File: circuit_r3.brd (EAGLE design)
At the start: 57.3 x 43.2 mm, 24 parts, among them IC1 7805DT, U1 MCP4725, U2 MB85RC256VPF-G-JNERE2, U4 ATMEGA328P_VQFNVQFN, Y1 16MHz

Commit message: Oooh, getting close.
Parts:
- removed C7: 0.1uF, custom:0603
- added J1: (no value), SparkFun-Connectors:6_PIN_SERIAL_TARGET_SIDE_W_SILK
- moved C5 90.6 mm to (47.0, 47.0), turned to 180 degrees
- moved C6 89.5 mm to (47.0, 41.9), turned to 180 degrees
- moved R5 85.0 mm to (47.0, 44.5), turned to 180 degrees
- moved C2 62.9 mm to (68.6, 39.2), turned to 270 degrees
- moved R1 62.6 mm to (61.2, 31.5), turned to 315 degrees
- moved U1 60.8 mm to (65.8, 39.0), turned to 270 degrees
- moved U2 58.9 mm to (62.2, 43.2), turned to 90 degrees
- moved R4 56.8 mm to (65.8, 35.4), turned to 180 degrees
- moved 12V 52.7 mm to (54.6, 24.1)
- moved U4 50.4 mm to (57.1, 35.6), turned to 45 degrees
- moved C4 46.7 mm to (61.6, 26.6), turned to 45 degrees
- moved R3 46.0 mm to (58.4, 47.0), turned to 90 degrees
- moved R6 45.7 mm to (56.4, 31.9), turned to 225 degrees
- moved ETH_PWR 45.1 mm to (50.8, 24.1)
- moved Y1 44.1 mm to (59.1, 29.2), turned to 135 degrees
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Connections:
- removed net AREF: C7.1, U4.17
- new net RXI: J1.P$2, U4.26
- new net TXO: J1.P$3, U4.27
- net DTR: now also J1.P$1
- net GND: now also J1.P$5, J1.P$6; no longer C7.2
- net VCC: now also J1.P$4
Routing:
- net GND: track 0.00 -> 48.2 mm, vias 0 -> 5
- net VCC: track 0.00 -> 31.7 mm, vias 0 -> 6
- net OUT: track 0.00 -> 26.4 mm, vias 0 -> 1
- net SCL: track 0.00 -> 26.1 mm, vias 0 -> 2
- net ETH: track 0.00 -> 24.9 mm, vias 0 -> 1
- net SDA: track 0.00 -> 19.5 mm
- net TXO: track 0.00 -> 14.7 mm, vias 0 -> 1
- net RXI: track 0.00 -> 13.3 mm, vias 0 -> 1
- net RESET: track 0.00 -> 12.9 mm
- net XT2: track 0.00 -> 11.7 mm
- net DTR: track 0.00 -> 10.8 mm
- net XT1: track 0.00 -> 9.59 mm
- net VIN: track 0.00 -> 9.25 mm
- net PD_L: track 0.00 -> 2.79 mm
- added copper zone on layer 2, net GND
- added copper zone on layer 15, net VCC
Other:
- board size 57.3 x 43.2 mm -> 160 x 100 mm

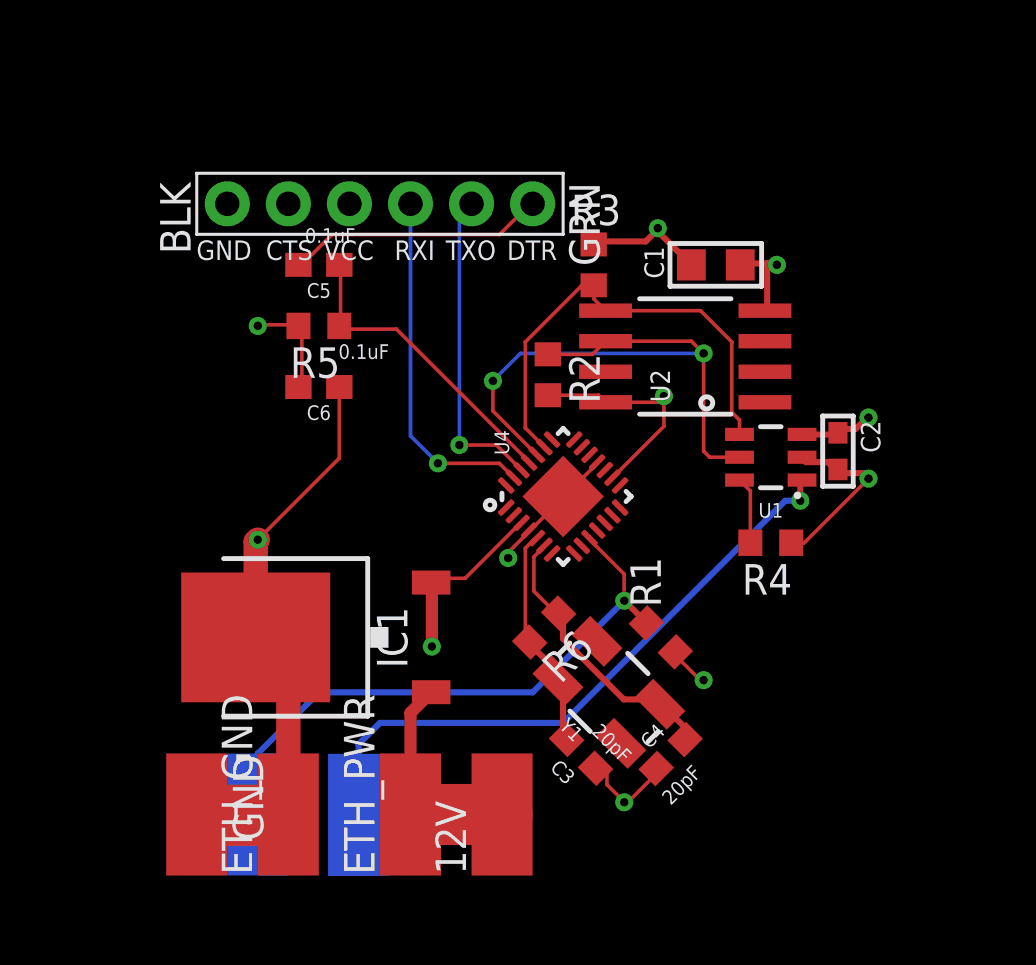
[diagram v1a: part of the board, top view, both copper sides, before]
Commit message: trying to make it smaller.
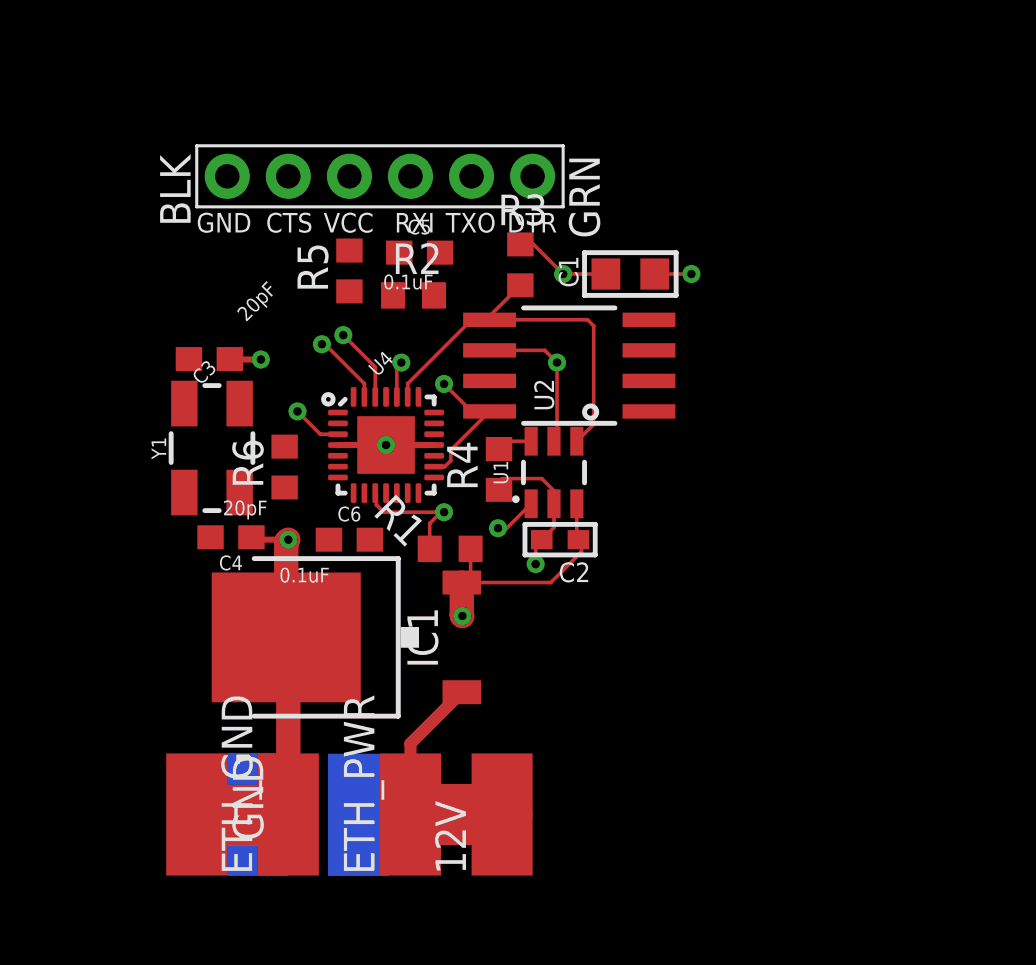
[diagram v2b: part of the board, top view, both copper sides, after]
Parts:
- moved C3 22.6 mm to (42.4, 43.1), turned to 180 degrees
- moved C4 20.4 mm to (43.3, 35.7), turned to 180 degrees
- moved Y1 19.4 mm to (42.5, 39.4), turned to 90 degrees
- moved R6 12.7 mm to (45.6, 38.6), turned to 90 degrees
- moved C2 12.1 mm to (57.0, 35.6), turned to 180 degrees
- moved R4 11.7 mm to (54.5, 38.5), turned to 90 degrees
- moved R1 9.51 mm to (52.5, 35.2), turned to 0 degrees
- moved U1 9.04 mm to (56.8, 38.4), turned to 180 degrees
- moved U4 9.04 mm to (48.5, 38.2), turned to 0 degrees
- moved R2 6.49 mm to (50.9, 45.7), turned to 0 degrees
- moved C6 6.48 mm to (48.3, 35.6), turned to 0 degrees
- moved U2 4.84 mm to (57.4, 42.8)
- moved C5 4.22 mm to (51.2, 47.5), turned to 0 degrees
- moved C1 3.58 mm to (59.9, 46.6)
- moved R3 3.05 mm to (55.4, 47.0)
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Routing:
- net OUT: track 26.4 -> 1.80 mm
- net ETH: track 24.9 -> 5.17 mm
- net SCL: track 26.1 -> 7.85 mm
- net GND: track 48.2 -> 32.3 mm
- net RESET: track 12.9 -> 0.00 mm
- net XT2: track 11.7 -> 0.00 mm
- net TXO: track 14.7 -> 3.00 mm
- net DTR: track 10.8 -> 0.00 mm
- net XT1: track 9.59 -> 0.00 mm
- net RXI: track 13.3 -> 3.84 mm
- net VCC: track 31.7 -> 22.8 mm, vias 6 -> 4
- net SDA: track 19.5 -> 15.6 mm
- net PD_L: track 2.79 -> 1.47 mm
- net VIN: track 9.25 -> 9.78 mm

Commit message: pre autoroute
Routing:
- net ETH: track 5.17 -> 21.0 mm
- net OUT: track 1.80 -> 16.1 mm
- net TXO: track 3.00 -> 11.5 mm
- net RXI: track 3.84 -> 11.9 mm
- net RESET: track 0.00 -> 5.02 mm
- net SCL: track 7.85 -> 10.8 mm
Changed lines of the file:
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@@
 <wire x1="56.896" y1="42.926" x2="56.896" y2="39.7811" width="0.1524" layer="1"/>
 <wire x1="56.896" y1="39.7811" x2="56.769" y2="39.6541" width="0.1524" layer="1"/>
-<wire x1="50.419" y1="42.926" x2="50.077" y2="45.72" width="0" layer="19" extent="1-1"/>
-<wire x1="54.089" y1="43.434" x2="50.419" y2="42.926" width="0" layer="19" extent="1-1"/>
+<wire x1="50.077" y1="45.72" x2="50.419" y2="45.378" width="0.1524" layer="1"/>
+<wire x1="50.419" y1="45.378" x2="50.419" y2="42.926" width="0.1524" layer="1"/>
+<wire x1="50.419" y1="42.926" x2="54.089" y2="43.434" width="0" layer="19" extent="1-1"/>
 </signal>
 <signal name="ETH">
@@
 <wire x1="51.601" y1="35.179" x2="51.601" y2="36.234" width="0.1524" layer="1"/>
 <wire x1="51.601" y1="36.234" x2="52.07" y2="36.703" width="0.1524" layer="1"/>
-<wire x1="44.45" y1="24.13" x2="51.601" y2="35.179" width="0" layer="19" extent="1-16"/>
+<wire x1="52.197" y1="36.703" x2="52.197" y2="34.417" width="0.1524" layer="16"/>
+<wire x1="52.197" y1="34.417" x2="44.45" y2="26.67" width="0.1524" layer="16"/>
+<wire x1="44.45" y1="26.67" x2="44.45" y2="24.13" width="0.1524" layer="16"/>
 </signal>
 <signal name="PD_L">
@@
 <wire x1="55.819" y1="37.0539" x2="54.8011" y2="36.036" width="0.1524" layer="1"/>
 <wire x1="54.8011" y1="36.036" x2="54.441" y2="36.036" width="0.1524" layer="1"/>
-<wire x1="48.641" y1="24.111946875" x2="54.441" y2="36.036" width="0" layer="19" extent="16-16"/>
+<wire x1="54.441" y1="36.036" x2="54.441" y2="29.911946875" width="0.1524" layer="16"/>
+<wire x1="54.441" y1="29.911946875" x2="48.641" y2="24.111946875" width="0.1524" layer="16"/>
 </signal>
 <signal name="XT1">
@@
 <contactref element="C5" pad="1"/>
 <contactref element="U4" pad="25"/>
-<wire x1="50.331" y1="47.498" x2="48.26" y2="45.886" width="0" layer="19" extent="1-1"/>
-<wire x1="49.784" y1="41.497" x2="48.26" y2="45.886" width="0" layer="19" extent="1-1"/>
+<wire x1="49.784" y1="41.497" x2="49.7352" y2="41.5458" width="0.1524" layer="1"/>
+<wire x1="48.26" y1="44.7475375" x2="48.26" y2="45.886" width="0.1524" layer="1"/>
+<wire x1="49.7352" y1="41.5458" x2="49.7352" y2="43.2723375" width="0.1524" layer="1"/>
+<wire x1="49.7352" y1="43.2723375" x2="48.26" y2="44.7475375" width="0.1524" layer="1"/>
+<wire x1="48.26" y1="45.886" x2="50.331" y2="47.498" width="0" layer="19" extent="1-1"/>
 </signal>
 <signal name="DTR">
@@
 <contactref element="J1" pad="P$2"/>
 <via x="48.006" y="44.069" extent="1-16" drill="0.35"/>
-<wire x1="52.832" y1="50.165" x2="53.34" y2="50.673" width="0.1524" layer="16"/>
 <wire x1="49.334" y1="41.497" x2="49.334" y2="42.741" width="0.1524" layer="1"/>
 <wire x1="49.334" y1="42.741" x2="48.006" y2="44.069" width="0.1524" layer="1"/>
-<wire x1="48.006" y1="44.069" x2="52.832" y2="50.165" width="0" layer="19" extent="16-16"/>
+<wire x1="48.006" y1="44.069" x2="48.006" y2="45.339" width="0.1524" layer="16"/>
+<wire x1="48.006" y1="45.339" x2="53.34" y2="50.673" width="0.1524" layer="16"/>
 </signal>
 <signal name="TXO">
@@
 <wire x1="47.244" y1="43.688" x2="47.117" y2="43.688" width="0.1524" layer="1"/>
 <wire x1="48.884" y1="42.048" x2="47.244" y2="43.688" width="0.1524" layer="1"/>
-<wire x1="47.244" y1="43.688" x2="50.8" y2="50.673" width="0" layer="19" extent="1-1"/>
+<wire x1="47.117" y1="43.688" x2="47.117" y2="46.99" width="0.1524" layer="16"/>
+<wire x1="47.117" y1="46.99" x2="50.8" y2="50.673" width="0.1524" layer="16"/>
 </signal>
 </signals>

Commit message: More revisions...
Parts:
- added J2: (no value), SparkFun-Connectors:2X3
- moved J1 13.8 mm to (37.8, 43.3), turned to 270 degrees
- moved C5 9.78 mm to (41.4, 47.4), turned to 90 degrees
- moved R3 7.77 mm to (47.8, 48.5), turned to 180 degrees
- moved C1 7.01 mm to (54.0, 50.3)
- moved R5 5.14 mm to (43.2, 47.5)
- moved U2 5.13 mm to (54.0, 46.6)
- moved R4 4.47 mm to (57.0, 42.2)
- moved U1 4.44 mm to (54.5, 42.2)
- moved C2 3.92 mm to (55.4, 39.1)
- moved R2 3.27 mm to (47.8, 46.5), turned to 180 degrees
- moved U4 1.27 mm to (48.5, 39.5)
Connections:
- new net ISP_MISO: J2.6, U4.14
- new net ISP_MOSI: J2.3, U4.13
- new net ISP_SCK: J2.4, U4.15
- net GND: now also J2.1
- net RESET: now also J2.2
- net VCC: now also J2.5
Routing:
- net RESET: track 5.02 -> 24.1 mm, vias 0 -> 2
- net VCC: track 22.8 -> 30.0 mm
- net ETH: track 21.0 -> 16.7 mm
- net DTR: track 0.00 -> 4.15 mm
- net SDA: track 15.6 -> 19.5 mm, vias 0 -> 2
- net SCL: track 10.8 -> 14.3 mm
- net GND: track 32.3 -> 28.9 mm, vias 5 -> 3
- net PD_L: track 1.47 -> 4.22 mm
- net OUT: track 16.1 -> 18.8 mm
- net RXI: track 11.9 -> 13.7 mm
- net ISP_MISO: track 0.00 -> 1.20 mm, vias 0 -> 1
- net ISP_SCK: track 0.00 -> 1.20 mm, vias 0 -> 1
- net ISP_MOSI: track 0.00 -> 1.18 mm, vias 0 -> 1
- net TXO: track 11.5 -> 12.1 mm

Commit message: Pretty good design.
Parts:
- added L_PGM: GREEN, SparkFun-LED:LED-0603
- added L_PWR: RED, SparkFun-LED:LED-0603
- added L_SNS: BLUE, SparkFun-LED:LED-0603
- added R7, R8: 10k, adafruit:R0603
- moved C1 45.2 mm to (13.6, 30.0)
- moved C2 44.0 mm to (16.4, 18.7)
- moved C3 44.0 mm to (3.45, 22.6)
- moved ETH 44.0 mm to (5.46, 3.68)
- moved IC1 44.0 mm to (9.14, 11.0)
- moved R1 44.0 mm to (13.5, 14.7)
- moved R2 44.0 mm to (8.76, 26.0)
- moved R3 44.0 mm to (8.76, 28.1)
- moved R4 44.0 mm to (18.0, 21.7)
- moved U2 44.0 mm to (15.0, 26.2)
- moved U4 44.0 mm to (9.53, 19.1)
- moved Y1 44.0 mm to (3.56, 18.9)
- moved 12V 44.0 mm to (15.6, 3.68)
- moved C4 44.0 mm to (4.35, 15.2)
- moved C6 44.0 mm to (9.27, 15.1)
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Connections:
- new net LED_GND: L_PGM.C, L_PWR.C, R8.1
- new net N$2: L_SNS.C, R7.2
- new net SENS_IND: L_SNS.A, U4.1
- net GND: now also R7.1, R8.2
- net ISP_SCK: now also L_PGM.A
- net VCC: now also L_PWR.A
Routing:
- net ISP_SCK: track 1.20 -> 22.9 mm
- net GND: track 28.9 -> 43.8 mm, vias 3 -> 7
- net ISP_MISO: track 1.20 -> 13.9 mm
- net VCC: track 30.0 -> 42.1 mm, vias 4 -> 3
- net ISP_MOSI: track 1.18 -> 11.3 mm
- net XT1: track 0.00 -> 9.54 mm
- net RESET: track 24.1 -> 32.8 mm, vias 2 -> 1
- net SENS_IND: track 0.00 -> 7.82 mm
- net XT2: track 0.00 -> 7.68 mm
- net LED_GND: track 0.00 -> 4.38 mm
- net ETH: track 16.7 -> 20.2 mm
- net N$2: track 0.00 -> 2.18 mm
- net DTR: track 4.15 -> 2.48 mm
- net TXO: track 12.1 -> 13.4 mm
- net RXI: track 13.7 -> 12.7 mm
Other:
- board size 160 x 100 mm -> 21.8 x 46.8 mm

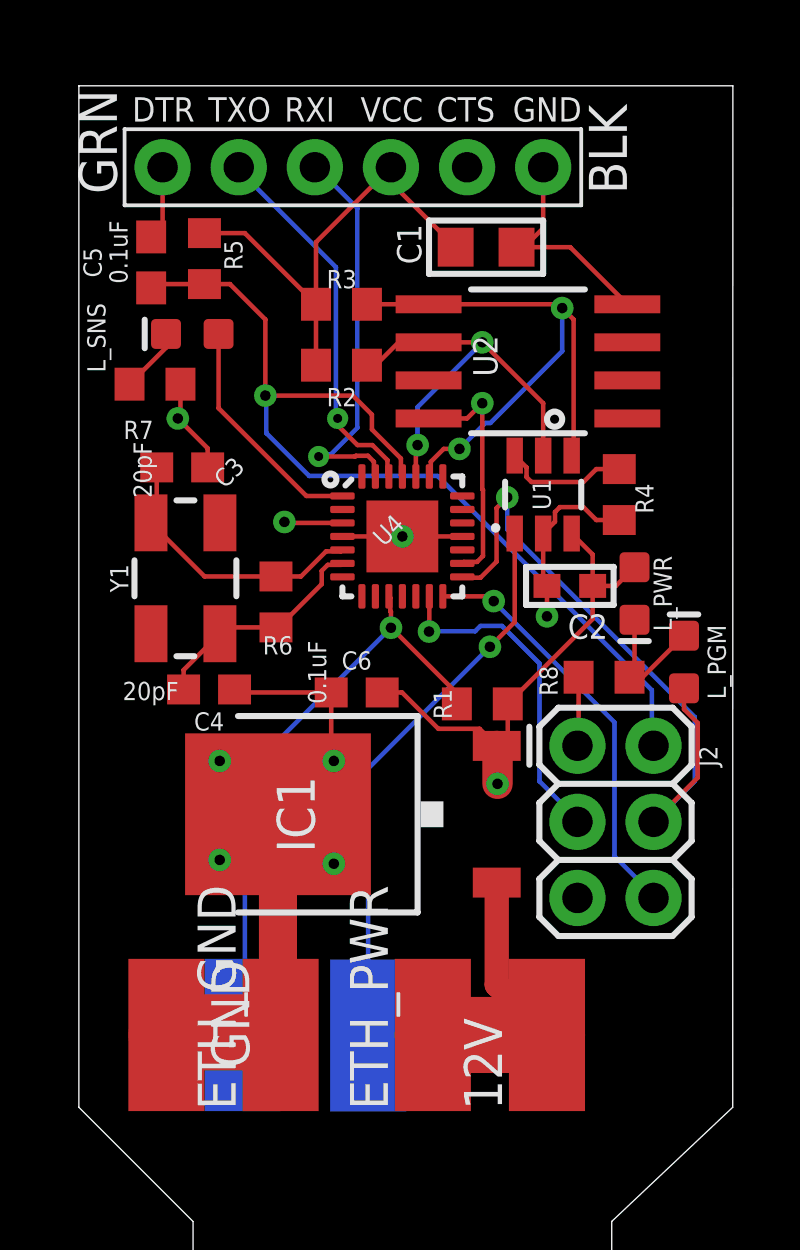
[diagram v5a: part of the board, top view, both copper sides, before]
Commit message: Production prototype, including indicator leds.
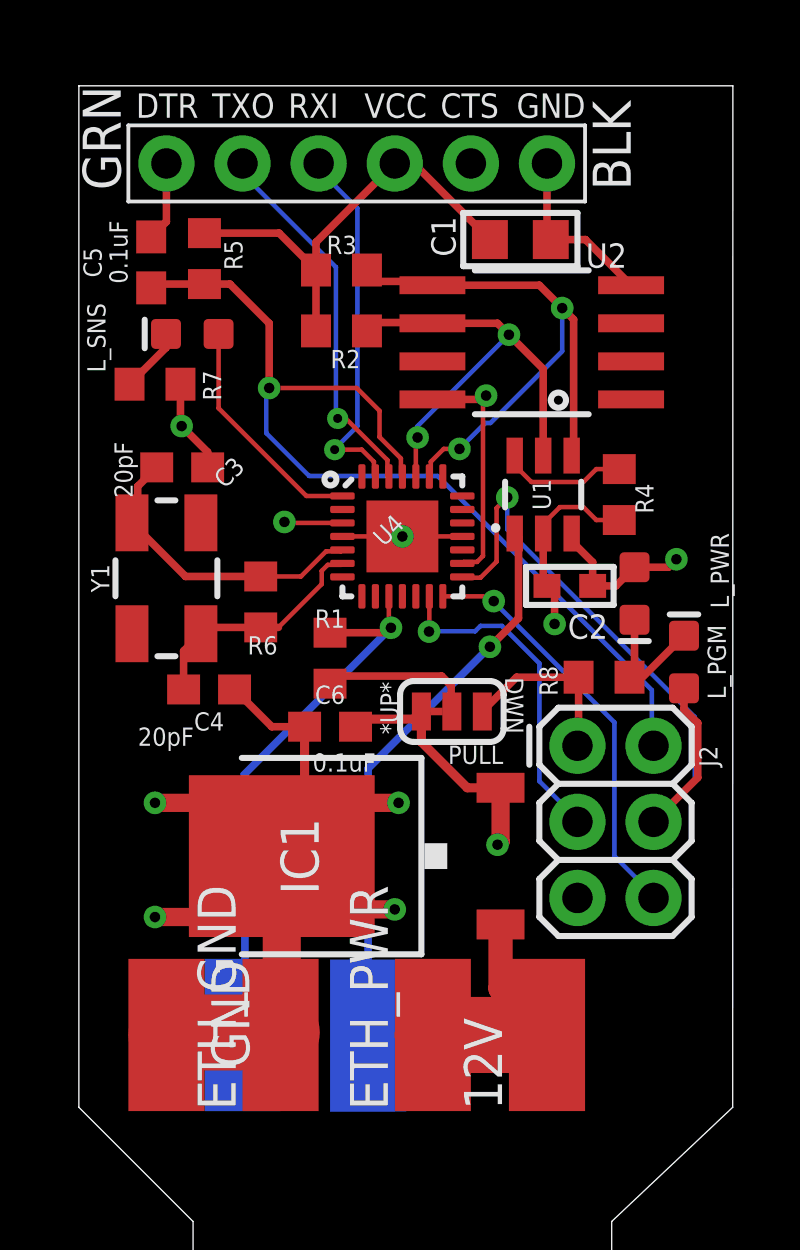
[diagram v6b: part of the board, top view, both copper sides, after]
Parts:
- added PULL: JUMPER-SMT_3_1-NC_TRACE_SILK, SparkFun-Jumpers:SMT-JUMPER_3_1-NC_TRACE_SILK
- L_PGM: value GREEN -> RED
- L_PWR: value RED -> GREEN
- R7: value 10k -> 100
- R8: value 10k -> 150
- moved R1 5.30 mm to (8.38, 16.3), turned to 270 degrees
- moved C6 1.45 mm to (8.38, 14.0)
- moved IC1 1.40 mm to (9.27, 9.65)
- moved C1 1.17 mm to (14.7, 30.2)
- moved R2 1.14 mm to (8.76, 27.2)
- moved R3 1.14 mm to (8.76, 29.2)
- moved U2 0.65 mm to (15.1, 26.8)
- moved Y1 0.64 mm to (2.92, 18.9)
- moved R6 0.51 mm to (6.07, 18.1)
- moved J1 0.18 mm to (9.27, 32.8)
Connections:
- new net ETHP: PULL.2, R1.2
- net GND: now also PULL.1
- net VCC: now also PULL.3; no longer R1.2
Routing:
- net GND: track 43.8 -> 64.1 mm
- net ETHP: track 0.00 -> 5.15 mm
- net VCC: track 42.1 -> 39.2 mm, vias 3 -> 4
- net VIN: track 9.59 -> 8.14 mm
- net ETH: track 20.2 -> 18.9 mm
- net SCL: track 14.3 -> 15.5 mm
- net TXO: track 13.4 -> 12.4 mm
- net XT1: track 9.54 -> 10.4 mm
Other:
- board text added: "*UP*"
- board text added: "DWN"
